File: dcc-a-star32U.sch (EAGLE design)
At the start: 7 parts, among them Q1 MOSFET-NCHANNEL2N7002PW

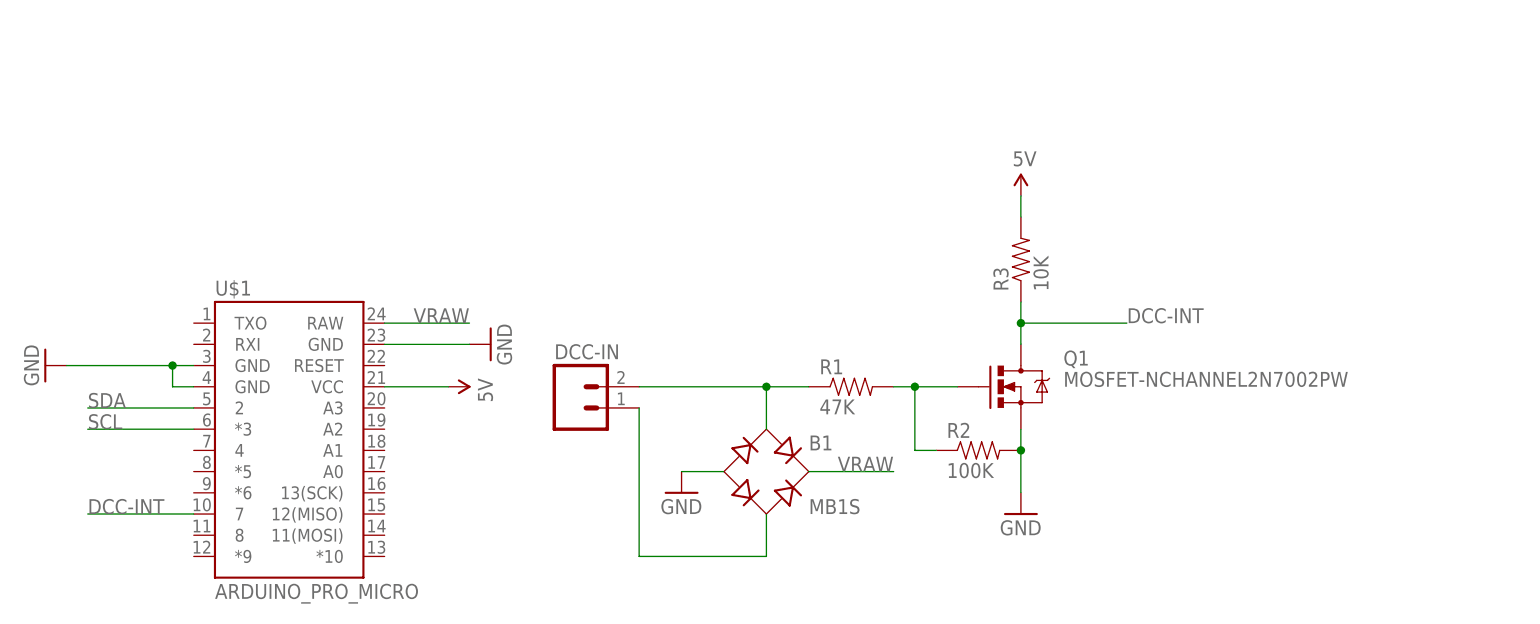
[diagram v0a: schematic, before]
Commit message: add a-star variant, use JST for dcc-powered boards
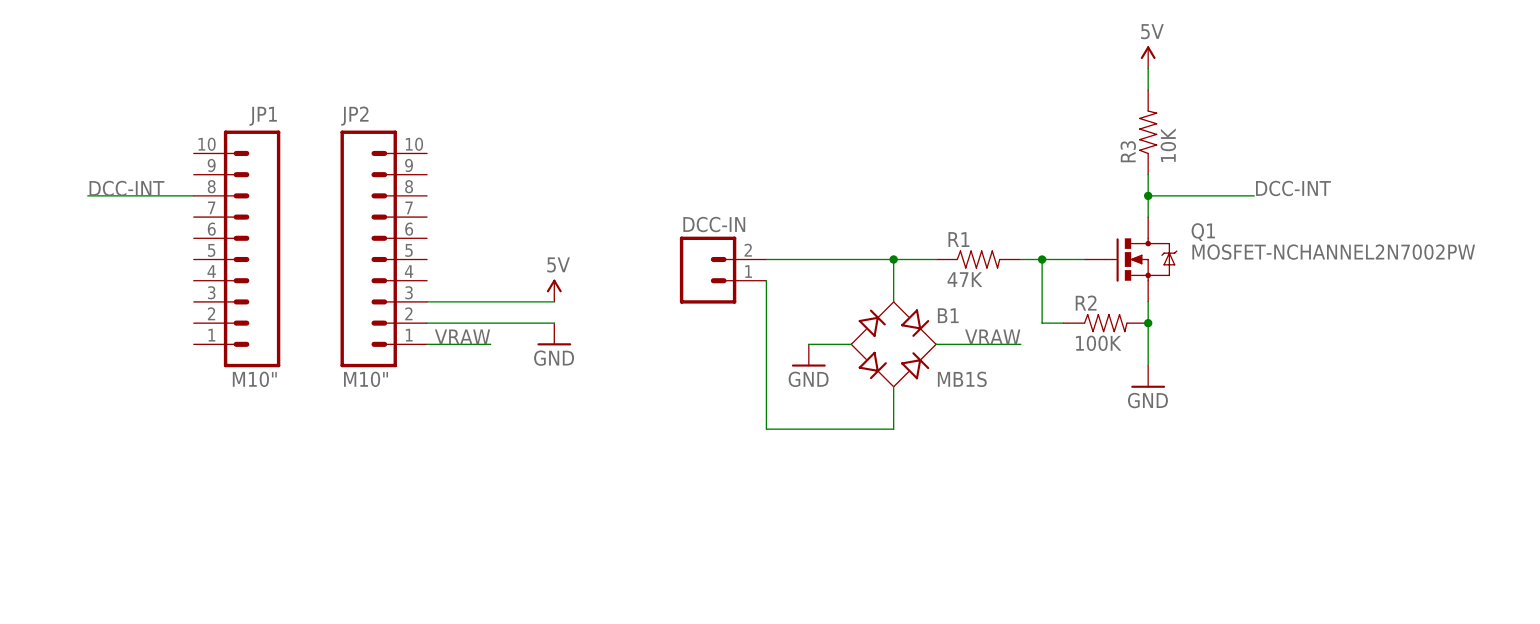
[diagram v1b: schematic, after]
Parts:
- removed U$1: ARDUINO_PRO_MICRO, SparkFun-Boards:ARDUINO_PRO_MICRO
- added JP1, JP2: M10", SparkFun-Connectors:M10"
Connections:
- removed net SCL: U$1.*3
- removed net SDA: U$1.2
- net 5V: now also JP2.3; no longer U$1.VCC
- net DCC-INT: now also JP1.8; no longer U$1.7
- net GND: now also JP2.2; no longer U$1.GND, U$1.GND@1, U$1.GND@2
- net VRAW: now also JP2.1; no longer U$1.RAW
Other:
- moved on the sheet: B1, DCC-IN, Q1, R1, R2, R3
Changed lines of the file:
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@@
 <parts>
 <part name="DCC-IN" library="SparkFun-Connectors" deviceset="M02" device="-JST-2-PTH-NO_SILK" value="M02-JST-2-PTH-NO_SILK"/>
-<part name="U$1" library="SparkFun-Boards" deviceset="ARDUINO_PRO_MICRO" device=""/>
-<part name="GND4" library="SparkFun-Aesthetics" deviceset="GND" device=""/>
 <part name="SUPPLY1" library="SparkFun-Aesthetics" deviceset="5V" device=""/>
 <part name="B1" library="rectifier" deviceset="MB*S" device="" technology="1"/>
@@
 <part name="R2" library="SparkFun-Passives" deviceset="RESISTOR" device="0603-RES" value="100K"/>
 <part name="GND3" library="SparkFun-Aesthetics" deviceset="GND" device=""/>
+<part name="JP1" library="SparkFun-Connectors" deviceset="M10" device="&quot;"/>
+<part name="JP2" library="SparkFun-Connectors" deviceset="M10" device="&quot;"/>
 </parts>
 <sheets>
@@
 </plain>
 <instances>
-<instance part="DCC-IN" gate="G$1" x="68.58" y="60.96" smashed="yes">
-<attribute name="NAME" x="66.04" y="66.802" size="1.778" layer="95"/>
+<instance part="DCC-IN" gate="G$1" x="83.82" y="76.2" smashed="yes">
+<attribute name="NAME" x="81.28" y="82.042" size="1.778" layer="95"/>
 </instance>
-<instance part="U$1" gate="G$1" x="33.02" y="55.88"/>
-<instance part="GND4" gate="1" x="5.08" y="66.04" rot="R270"/>
-<instance part="SUPPLY1" gate="G$1" x="53.34" y="63.5" rot="R270"/>
-<instance part="B1" gate="G$1" x="91.44" y="53.34"/>
-<instance part="GND1" gate="1" x="81.28" y="50.8"/>
-<instance part="R1" gate="G$1" x="101.6" y="63.5"/>
-<instance part="Q1" gate="G$1" x="121.92" y="63.5"/>
-<instance part="SUPPLY2" gate="G$1" x="121.92" y="86.36"/>
-<instance part="R3" gate="G$1" x="121.92" y="78.74" rot="R90"/>
-<instance part="GND2" gate="1" x="121.92" y="48.26"/>
-<instance part="R2" gate="G$1" x="116.84" y="55.88"/>
-<instance part="GND3" gate="1" x="58.42" y="68.58" rot="R90"/>
+<instance part="SUPPLY1" gate="G$1" x="66.04" y="73.66"/>
+<instance part="B1" gate="G$1" x="106.68" y="68.58"/>
+<instance part="GND1" gate="1" x="96.52" y="66.04"/>
+<instance part="R1" gate="G$1" x="116.84" y="78.74"/>
+<instance part="Q1" gate="G$1" x="137.16" y="78.74"/>
+<instance part="SUPPLY2" gate="G$1" x="137.16" y="101.6"/>
+<instance part="R3" gate="G$1" x="137.16" y="93.98" rot="R90"/>
+<instance part="GND2" gate="1" x="137.16" y="63.5"/>
+<instance part="R2" gate="G$1" x="132.08" y="71.12"/>
+<instance part="GND3" gate="1" x="66.04" y="68.58"/>
+<instance part="JP1" gate="G$1" x="33.02" y="86.36" rot="MR0"/>
+<instance part="JP2" gate="G$1" x="40.64" y="86.36"/>
 </instances>
 <busses>
@@
 <net name="GND" class="0">
 <segment>
-<pinref part="U$1" gate="G$1" pin="GND"/>
-<wire x1="22.86" y1="63.5" x2="20.32" y2="63.5" width="0.1524" layer="91"/>
-<wire x1="20.32" y1="63.5" x2="20.32" y2="66.04" width="0.1524" layer="91"/>
-<pinref part="U$1" gate="G$1" pin="GND@1"/>
-<wire x1="22.86" y1="66.04" x2="20.32" y2="66.04" width="0.1524" layer="91"/>
-<wire x1="20.32" y1="66.04" x2="7.62" y2="66.04" width="0.1524" layer="91"/>
-<pinref part="GND4" gate="1" pin="GND"/>
-<junction x="20.32" y="66.04"/>
-</segment>
-<segment>
 <pinref part="B1" gate="G$1" pin="-"/>
-<wire x1="86.36" y1="53.34" x2="81.28" y2="53.34" width="0.1524" layer="91"/>
+<wire x1="101.6" y1="68.58" x2="96.52" y2="68.58" width="0.1524" layer="91"/>
 <pinref part="GND1" gate="1" pin="GND"/>
 </segment>
 <segment>
 <pinref part="Q1" gate="G$1" pin="S"/>
-<wire x1="121.92" y1="58.42" x2="121.92" y2="55.88" width="0.1524" layer="91"/>
+<wire x1="137.16" y1="73.66" x2="137.16" y2="71.12" width="0.1524" layer="91"/>
 <pinref part="GND2" gate="1" pin="GND"/>
 <pinref part="R2" gate="G$1" pin="2"/>
-<wire x1="121.92" y1="55.88" x2="121.92" y2="50.8" width="0.1524" layer="91"/>
-<junction x="121.92" y="55.88"/>
+<wire x1="137.16" y1="71.12" x2="137.16" y2="66.04" width="0.1524" layer="91"/>
+<junction x="137.16" y="71.12"/>
 </segment>
 <segment>
 <pinref part="GND3" gate="1" pin="GND"/>
-<pinref part="U$1" gate="G$1" pin="GND@2"/>
-<wire x1="55.88" y1="68.58" x2="45.72" y2="68.58" width="0.1524" layer="91"/>
+<wire x1="50.8" y1="71.12" x2="66.04" y2="71.12" width="0.1524" layer="91"/>
+<pinref part="JP2" gate="G$1" pin="2"/>
 </segment>
 </net>
 <net name="DCC-INT" class="0">
 <segment>
-<pinref part="U$1" gate="G$1" pin="7"/>
-<wire x1="22.86" y1="48.26" x2="10.16" y2="48.26" width="0.1524" layer="91"/>
-<label x="10.16" y="48.26" size="1.778" layer="95"/>
+<label x="10.16" y="86.36" size="1.778" layer="95"/>
+<pinref part="JP1" gate="G$1" pin="8"/>
+<wire x1="22.86" y1="86.36" x2="10.16" y2="86.36" width="0.1524" layer="91"/>
 </segment>
 <segment>
 <pinref part="Q1" gate="G$1" pin="D"/>
 <pinref part="R3" gate="G$1" pin="1"/>
-<wire x1="121.92" y1="73.66" x2="121.92" y2="71.12" width="0.1524" layer="91"/>
-<wire x1="121.92" y1="71.12" x2="121.92" y2="68.58" width="0.1524" layer="91"/>
-<wire x1="121.92" y1="71.12" x2="134.62" y2="71.12" width="0.1524" layer="91"/>
-<junction x="121.92" y="71.12"/>
-<label x="134.62" y="71.12" size="1.778" layer="95"/>
+<wire x1="137.16" y1="88.9" x2="137.16" y2="86.36" width="0.1524" layer="91"/>
+<wire x1="137.16" y1="86.36" x2="137.16" y2="83.82" width="0.1524" layer="91"/>
+<wire x1="137.16" y1="86.36" x2="149.86" y2="86.36" width="0.1524" layer="91"/>
+<junction x="137.16" y="86.36"/>
+<label x="149.86" y="86.36" size="1.778" layer="95"/>
 </segment>
 </net>
 <net name="5V" class="0">
 <segment>
-<pinref part="U$1" gate="G$1" pin="VCC"/>
-<wire x1="45.72" y1="63.5" x2="53.34" y2="63.5" width="0.1524" layer="91"/>
+<wire x1="50.8" y1="73.66" x2="66.04" y2="73.66" width="0.1524" layer="91"/>
 <pinref part="SUPPLY1" gate="G$1" pin="5V"/>
+<pinref part="JP2" gate="G$1" pin="3"/>
 </segment>
 <segment>
 <pinref part="SUPPLY2" gate="G$1" pin="5V"/>
 <pinref part="R3" gate="G$1" pin="2"/>
-<wire x1="121.92" y1="86.36" x2="121.92" y2="83.82" width="0.1524" layer="91"/>
-</segment>
-</net>
-<net name="SCL" class="0">
-<segment>
-<pinref part="U$1" gate="G$1" pin="*3"/>
-<wire x1="22.86" y1="58.42" x2="10.16" y2="58.42" width="0.1524" layer="91"/>
-<label x="10.16" y="58.42" size="1.778" layer="95"/>
-</segment>
-</net>
-<net name="SDA" class="0">
-<segment>
-<pinref part="U$1" gate="G$1" pin="2"/>
-<wire x1="22.86" y1="60.96" x2="10.16" y2="60.96" width="0.1524" layer="91"/>
-<label x="10.16" y="60.96" size="1.778" layer="95"/>
+<wire x1="137.16" y1="101.6" x2="137.16" y2="99.06" width="0.1524" layer="91"/>
 </segment>
 </net>
 <net name="VRAW" class="0">
 <segment>
-<pinref part="U$1" gate="G$1" pin="RAW"/>
-<wire x1="45.72" y1="71.12" x2="55.88" y2="71.12" width="0.1524" layer="91"/>
-<label x="55.88" y="71.12" size="1.778" layer="95" rot="MR0"/>
+<wire x1="50.8" y1="68.58" x2="58.42" y2="68.58" width="0.1524" layer="91"/>
+<label x="58.42" y="68.58" size="1.778" layer="95" rot="MR0"/>
+<pinref part="JP2" gate="G$1" pin="1"/>
 </segment>
 <segment>
 <pinref part="B1" gate="G$1" pin="+"/>
-<wire x1="96.52" y1="53.34" x2="106.68" y2="53.34" width="0.1524" layer="91"/>
-<label x="106.68" y="53.34" size="1.778" layer="95" rot="MR0"/>
+<wire x1="111.76" y1="68.58" x2="121.92" y2="68.58" width="0.1524" layer="91"/>
+<label x="121.92" y="68.58" size="1.778" layer="95" rot="MR0"/>
 </segment>
 </net>
@@
 <segment>
 <pinref part="B1" gate="G$1" pin="AC1"/>
-<wire x1="91.44" y1="58.42" x2="91.44" y2="63.5" width="0.1524" layer="91"/>
-<wire x1="91.44" y1="63.5" x2="76.2" y2="63.5" width="0.1524" layer="91"/>
+<wire x1="106.68" y1="73.66" x2="106.68" y2="78.74" width="0.1524" layer="91"/>
+<wire x1="106.68" y1="78.74" x2="91.44" y2="78.74" width="0.1524" layer="91"/>
 <pinref part="DCC-IN" gate="G$1" pin="2"/>
 <pinref part="R1" gate="G$1" pin="1"/>
-<wire x1="91.44" y1="63.5" x2="96.52" y2="63.5" width="0.1524" layer="91"/>
-<junction x="91.44" y="63.5"/>
+<wire x1="106.68" y1="78.74" x2="111.76" y2="78.74" width="0.1524" layer="91"/>
+<junction x="106.68" y="78.74"/>
 </segment>
 </net>
@@
 <segment>
 <pinref part="B1" gate="G$1" pin="AC2"/>
-<wire x1="91.44" y1="48.26" x2="91.44" y2="43.18" width="0.1524" layer="91"/>
-<wire x1="91.44" y1="43.18" x2="76.2" y2="43.18" width="0.1524" layer="91"/>
+<wire x1="106.68" y1="63.5" x2="106.68" y2="58.42" width="0.1524" layer="91"/>
+<wire x1="106.68" y1="58.42" x2="91.44" y2="58.42" width="0.1524" layer="91"/>
 <pinref part="DCC-IN" gate="G$1" pin="1"/>
-<wire x1="76.2" y1="60.96" x2="76.2" y2="43.18" width="0.1524" layer="91"/>
+<wire x1="91.44" y1="76.2" x2="91.44" y2="58.42" width="0.1524" layer="91"/>
 </segment>
 </net>
@@
 <segment>
 <pinref part="R1" gate="G$1" pin="2"/>
-<wire x1="106.68" y1="63.5" x2="109.22" y2="63.5" width="0.1524" layer="91"/>
+<wire x1="121.92" y1="78.74" x2="124.46" y2="78.74" width="0.1524" layer="91"/>
 <pinref part="Q1" gate="G$1" pin="G"/>
 <pinref part="R2" gate="G$1" pin="1"/>
-<wire x1="109.22" y1="63.5" x2="114.3" y2="63.5" width="0.1524" layer="91"/>
-<wire x1="111.76" y1="55.88" x2="109.22" y2="55.88" width="0.1524" layer="91"/>
-<wire x1="109.22" y1="55.88" x2="109.22" y2="63.5" width="0.1524" layer="91"/>
-<junction x="109.22" y="63.5"/>
+<wire x1="124.46" y1="78.74" x2="129.54" y2="78.74" width="0.1524" layer="91"/>
+<wire x1="127" y1="71.12" x2="124.46" y2="71.12" width="0.1524" layer="91"/>
+<wire x1="124.46" y1="71.12" x2="124.46" y2="78.74" width="0.1524" layer="91"/>
+<junction x="124.46" y="78.74"/>
 </segment>
 </net>
